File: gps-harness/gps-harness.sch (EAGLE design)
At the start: 7 parts

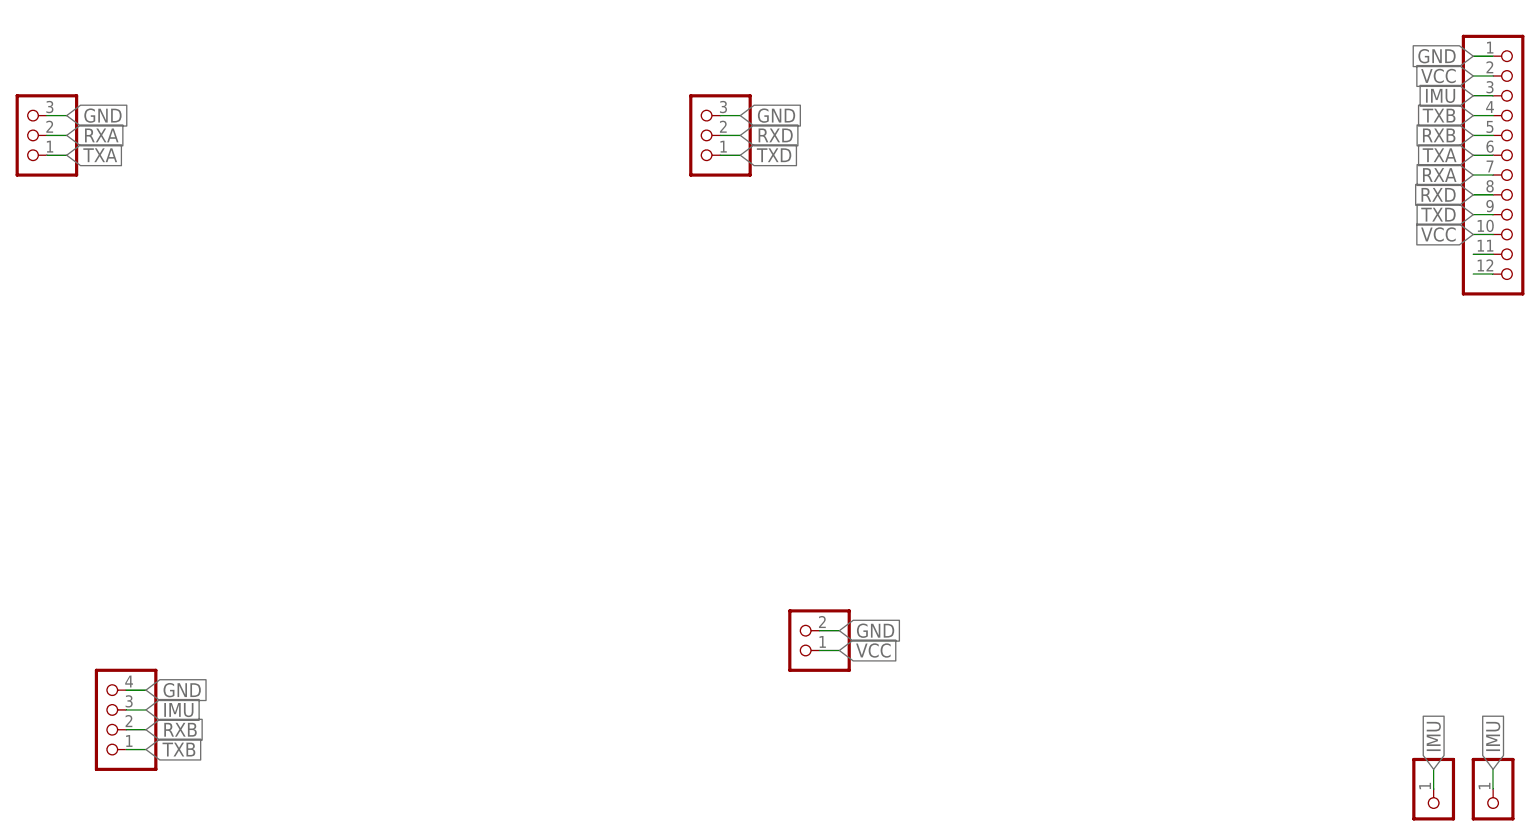
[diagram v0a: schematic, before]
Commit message: Add GND Plane
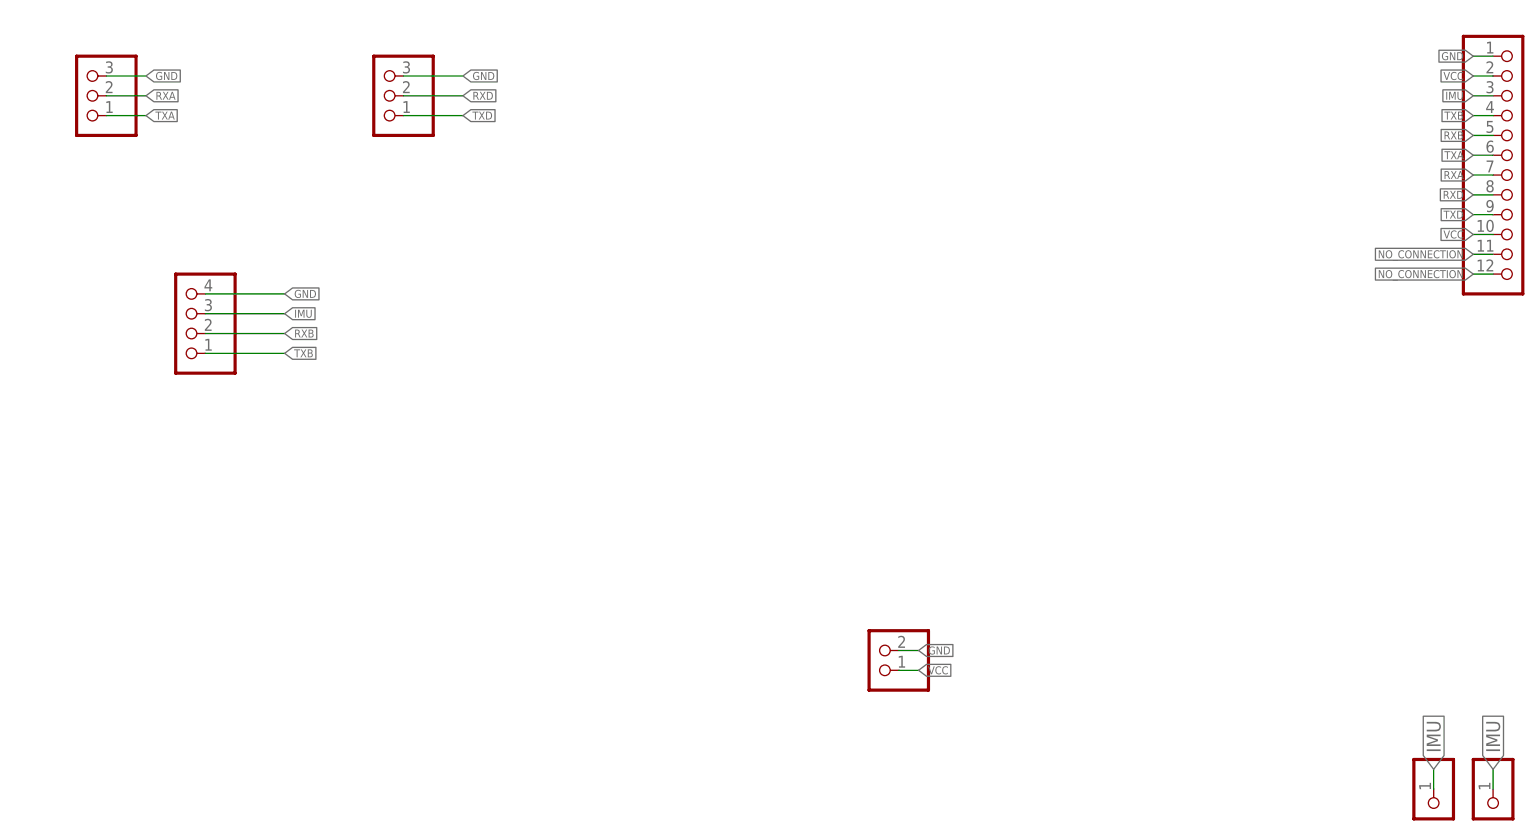
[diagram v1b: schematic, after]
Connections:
- removed net N$23: GPIO.11
- removed net N$24: GPIO.12
- new net NO_CONNECTION: GPIO.11, GPIO.12

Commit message: Add GND PLane & clearify the fastner of the right bottom driller, regorup rhe schematic
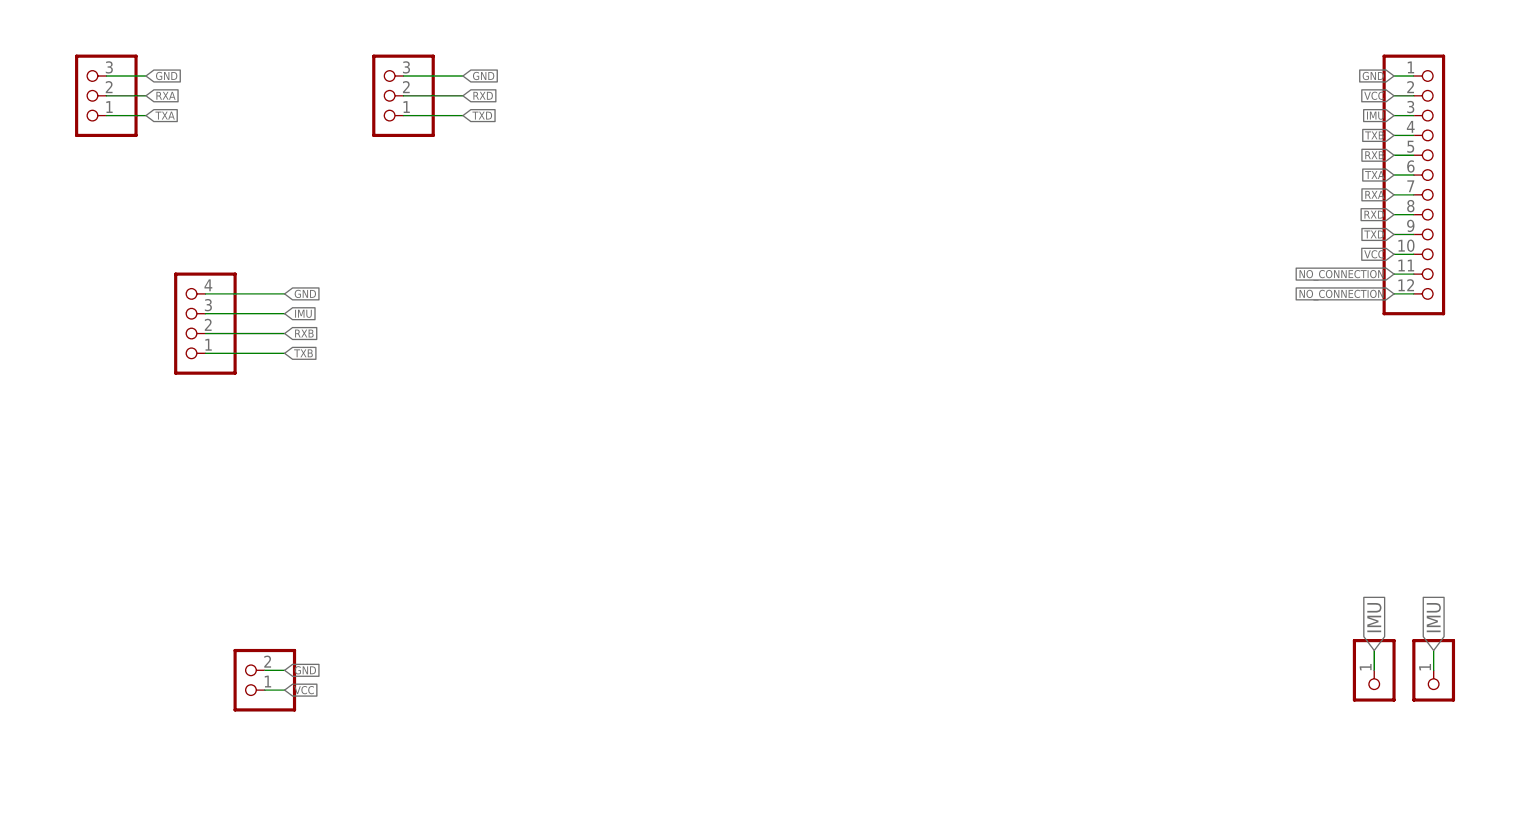
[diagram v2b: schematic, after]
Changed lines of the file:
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@@
 <attribute name="VALUE" x="59.69" y="157.48" size="1.778" layer="96" rot="R180"/>
 </instance>
-<instance part="BATTERY" gate="G$1" x="142.24" y="106.68" smashed="yes" rot="R180" grouprefs="BATTERY_POWER">
-<attribute name="VALUE" x="148.59" y="111.76" size="1.778" layer="96" rot="R180"/>
+<instance part="BATTERY" gate="G$1" x="60.96" y="104.14" smashed="yes" rot="R180" grouprefs="BATTERY_POWER">
+<attribute name="VALUE" x="67.31" y="109.22" size="1.778" layer="96" rot="R180"/>
 </instance>
-<instance part="GPIO" gate="G$1" x="223.52" y="170.18" smashed="yes" grouprefs="GPI/O">
-<attribute name="VALUE" x="217.17" y="149.86" size="1.778" layer="96"/>
+<instance part="GPIO" gate="G$1" x="213.36" y="167.64" smashed="yes" grouprefs="GPI/O">
+<attribute name="VALUE" x="207.01" y="147.32" size="1.778" layer="96"/>
 </instance>
-<instance part="IMU" gate="G$1" x="213.36" y="86.36" smashed="yes" rot="R270" grouprefs="IMU_TSY">
-<attribute name="VALUE" x="208.28" y="92.71" size="1.778" layer="96" rot="R270"/>
+<instance part="IMU" gate="G$1" x="205.74" y="101.6" smashed="yes" rot="R270" grouprefs="IMU_TSY">
+<attribute name="VALUE" x="200.66" y="107.95" size="1.778" layer="96" rot="R270"/>
 </instance>
-<instance part="TSY" gate="G$1" x="220.98" y="86.36" smashed="yes" rot="R270" grouprefs="IMU_TSY">
-<attribute name="VALUE" x="215.9" y="92.71" size="1.778" layer="96" rot="R270"/>
+<instance part="TSY" gate="G$1" x="213.36" y="101.6" smashed="yes" rot="R270" grouprefs="IMU_TSY">
+<attribute name="VALUE" x="208.28" y="107.95" size="1.778" layer="96" rot="R270"/>
 </instance>
 <instance part="FRAME1" gate="G$1" x="0" y="0" smashed="yes"/>
@@
 <segment>
 <pinref part="GPIO" gate="G$1" pin="1"/>
-<wire x1="220.98" y1="182.88" x2="218.44" y2="182.88" width="0.1524" layer="91" grouprefs="GPI/O"/>
-<label x="218.44" y="182.88" size="1.016" layer="95" rot="R180" xref="yes" grouprefs="GPI/O"/>
+<wire x1="210.82" y1="180.34" x2="208.28" y2="180.34" width="0.1524" layer="91" grouprefs="GPI/O"/>
+<label x="208.28" y="180.34" size="1.016" layer="95" rot="R180" xref="yes" grouprefs="GPI/O"/>
 </segment>
 <segment>
 <pinref part="BATTERY" gate="G$1" pin="2"/>
-<wire x1="144.78" y1="106.68" x2="147.32" y2="106.68" width="0.1524" layer="91" grouprefs="BATTERY_POWER"/>
-<label x="147.32" y="106.68" size="1.016" layer="95" xref="yes" grouprefs="BATTERY_POWER"/>
+<wire x1="63.5" y1="104.14" x2="66.04" y2="104.14" width="0.1524" layer="91" grouprefs="BATTERY_POWER"/>
+<label x="66.04" y="104.14" size="1.016" layer="95" xref="yes" grouprefs="BATTERY_POWER"/>
 </segment>
 </net>
@@
 <segment>
 <pinref part="GPIO" gate="G$1" pin="7"/>
-<wire x1="220.98" y1="167.64" x2="218.44" y2="167.64" width="0.1524" layer="91" grouprefs="GPI/O"/>
-<label x="218.44" y="167.64" size="1.016" layer="95" rot="R180" xref="yes" grouprefs="GPI/O"/>
+<wire x1="210.82" y1="165.1" x2="208.28" y2="165.1" width="0.1524" layer="91" grouprefs="GPI/O"/>
+<label x="208.28" y="165.1" size="1.016" layer="95" rot="R180" xref="yes" grouprefs="GPI/O"/>
 </segment>
 </net>
@@
 <segment>
 <pinref part="GPIO" gate="G$1" pin="6"/>
-<wire x1="220.98" y1="170.18" x2="218.44" y2="170.18" width="0.1524" layer="91" grouprefs="GPI/O"/>
-<label x="218.44" y="170.18" size="1.016" layer="95" rot="R180" xref="yes" grouprefs="GPI/O"/>
+<wire x1="210.82" y1="167.64" x2="208.28" y2="167.64" width="0.1524" layer="91" grouprefs="GPI/O"/>
+<label x="208.28" y="167.64" size="1.016" layer="95" rot="R180" xref="yes" grouprefs="GPI/O"/>
 </segment>
 </net>
@@
 <segment>
 <pinref part="GPIO" gate="G$1" pin="5"/>
-<wire x1="220.98" y1="172.72" x2="218.44" y2="172.72" width="0.1524" layer="91" grouprefs="GPI/O"/>
-<label x="218.44" y="172.72" size="1.016" layer="95" rot="R180" xref="yes" grouprefs="GPI/O"/>
+<wire x1="210.82" y1="170.18" x2="208.28" y2="170.18" width="0.1524" layer="91" grouprefs="GPI/O"/>
+<label x="208.28" y="170.18" size="1.016" layer="95" rot="R180" xref="yes" grouprefs="GPI/O"/>
 </segment>
 </net>
@@
 <segment>
 <pinref part="GPIO" gate="G$1" pin="4"/>
-<wire x1="220.98" y1="175.26" x2="218.44" y2="175.26" width="0.1524" layer="91" grouprefs="GPI/O"/>
-<label x="218.44" y="175.26" size="1.016" layer="95" rot="R180" xref="yes" grouprefs="GPI/O"/>
+<wire x1="210.82" y1="172.72" x2="208.28" y2="172.72" width="0.1524" layer="91" grouprefs="GPI/O"/>
+<label x="208.28" y="172.72" size="1.016" layer="95" rot="R180" xref="yes" grouprefs="GPI/O"/>
 </segment>
 </net>
@@
 <segment>
 <pinref part="BATTERY" gate="G$1" pin="1"/>
-<wire x1="144.78" y1="104.14" x2="147.32" y2="104.14" width="0.1524" layer="91" grouprefs="BATTERY_POWER"/>
-<label x="147.32" y="104.14" size="1.016" layer="95" xref="yes" grouprefs="BATTERY_POWER"/>
+<wire x1="63.5" y1="101.6" x2="66.04" y2="101.6" width="0.1524" layer="91" grouprefs="BATTERY_POWER"/>
+<label x="66.04" y="101.6" size="1.016" layer="95" xref="yes" grouprefs="BATTERY_POWER"/>
 </segment>
 <segment>
 <pinref part="GPIO" gate="G$1" pin="2"/>
-<wire x1="220.98" y1="180.34" x2="218.44" y2="180.34" width="0.1524" layer="91" grouprefs="GPI/O"/>
-<label x="218.44" y="180.34" size="1.016" layer="95" rot="R180" xref="yes" grouprefs="GPI/O"/>
+<wire x1="210.82" y1="177.8" x2="208.28" y2="177.8" width="0.1524" layer="91" grouprefs="GPI/O"/>
+<label x="208.28" y="177.8" size="1.016" layer="95" rot="R180" xref="yes" grouprefs="GPI/O"/>
 </segment>
 <segment>
 <pinref part="GPIO" gate="G$1" pin="10"/>
-<wire x1="220.98" y1="160.02" x2="218.44" y2="160.02" width="0.1524" layer="91" grouprefs="GPI/O"/>
-<label x="218.44" y="160.02" size="1.016" layer="95" rot="R180" xref="yes" grouprefs="GPI/O"/>
+<wire x1="210.82" y1="157.48" x2="208.28" y2="157.48" width="0.1524" layer="91" grouprefs="GPI/O"/>
+<label x="208.28" y="157.48" size="1.016" layer="95" rot="R180" xref="yes" grouprefs="GPI/O"/>
 </segment>
 </net>
@@
 <segment>
 <pinref part="GPIO" gate="G$1" pin="9"/>
-<wire x1="220.98" y1="162.56" x2="218.44" y2="162.56" width="0.1524" layer="91" grouprefs="GPI/O"/>
-<label x="218.44" y="162.56" size="1.016" layer="95" rot="R180" xref="yes" grouprefs="GPI/O"/>
+<wire x1="210.82" y1="160.02" x2="208.28" y2="160.02" width="0.1524" layer="91" grouprefs="GPI/O"/>
+<label x="208.28" y="160.02" size="1.016" layer="95" rot="R180" xref="yes" grouprefs="GPI/O"/>
 </segment>
 </net>
@@
 <segment>
 <pinref part="GPIO" gate="G$1" pin="8"/>
-<wire x1="220.98" y1="165.1" x2="218.44" y2="165.1" width="0.1524" layer="91" grouprefs="GPI/O"/>
-<label x="218.44" y="165.1" size="1.016" layer="95" rot="R180" xref="yes" grouprefs="GPI/O"/>
+<wire x1="210.82" y1="162.56" x2="208.28" y2="162.56" width="0.1524" layer="91" grouprefs="GPI/O"/>
+<label x="208.28" y="162.56" size="1.016" layer="95" rot="R180" xref="yes" grouprefs="GPI/O"/>
 </segment>
 </net>
@@
 <segment>
 <pinref part="GPIO" gate="G$1" pin="3"/>
-<wire x1="220.98" y1="177.8" x2="218.44" y2="177.8" width="0.1524" layer="91" grouprefs="GPI/O"/>
-<label x="218.44" y="177.8" size="1.016" layer="95" rot="R180" xref="yes" grouprefs="GPI/O"/>
+<wire x1="210.82" y1="175.26" x2="208.28" y2="175.26" width="0.1524" layer="91" grouprefs="GPI/O"/>
+<label x="208.28" y="175.26" size="1.016" layer="95" rot="R180" xref="yes" grouprefs="GPI/O"/>
 </segment>
 <segment>
@@
 <segment>
 <pinref part="IMU" gate="G$1" pin="1"/>
-<wire x1="213.36" y1="88.9" x2="213.36" y2="91.44" width="0.1524" layer="91" grouprefs="IMU_TSY"/>
-<label x="213.36" y="91.44" size="1.778" layer="95" rot="R90" xref="yes" grouprefs="IMU_TSY"/>
+<wire x1="205.74" y1="104.14" x2="205.74" y2="106.68" width="0.1524" layer="91" grouprefs="IMU_TSY"/>
+<label x="205.74" y="106.68" size="1.778" layer="95" rot="R90" xref="yes" grouprefs="IMU_TSY"/>
 </segment>
 <segment>
 <pinref part="TSY" gate="G$1" pin="1"/>
-<wire x1="220.98" y1="88.9" x2="220.98" y2="91.44" width="0.1524" layer="91" grouprefs="IMU_TSY"/>
-<label x="220.98" y="91.44" size="1.778" layer="95" rot="R90" xref="yes" grouprefs="IMU_TSY"/>
+<wire x1="213.36" y1="104.14" x2="213.36" y2="106.68" width="0.1524" layer="91" grouprefs="IMU_TSY"/>
+<label x="213.36" y="106.68" size="1.778" layer="95" rot="R90" xref="yes" grouprefs="IMU_TSY"/>
 </segment>
 </net>
@@
 <segment>
 <pinref part="GPIO" gate="G$1" pin="11"/>
-<wire x1="220.98" y1="157.48" x2="218.44" y2="157.48" width="0.1524" layer="91" grouprefs="GPI/O"/>
-<label x="218.44" y="157.48" size="1.016" layer="95" rot="R180" xref="yes"/>
+<wire x1="210.82" y1="154.94" x2="208.28" y2="154.94" width="0.1524" layer="91" grouprefs="GPI/O"/>
+<label x="208.28" y="154.94" size="1.016" layer="95" rot="R180" xref="yes"/>
 </segment>
 <segment>
 <pinref part="GPIO" gate="G$1" pin="12"/>
-<wire x1="220.98" y1="154.94" x2="218.44" y2="154.94" width="0.1524" layer="91" grouprefs="GPI/O"/>
-<label x="218.44" y="154.94" size="1.016" layer="95" rot="R180" xref="yes"/>
+<wire x1="210.82" y1="152.4" x2="208.28" y2="152.4" width="0.1524" layer="91" grouprefs="GPI/O"/>
+<label x="208.28" y="152.4" size="1.016" layer="95" rot="R180" xref="yes"/>
 </segment>
 </net>

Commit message: Modify the place of the left bottom mounting hole; Unify the width of the wires; clear up the GND line since there's a ground plane
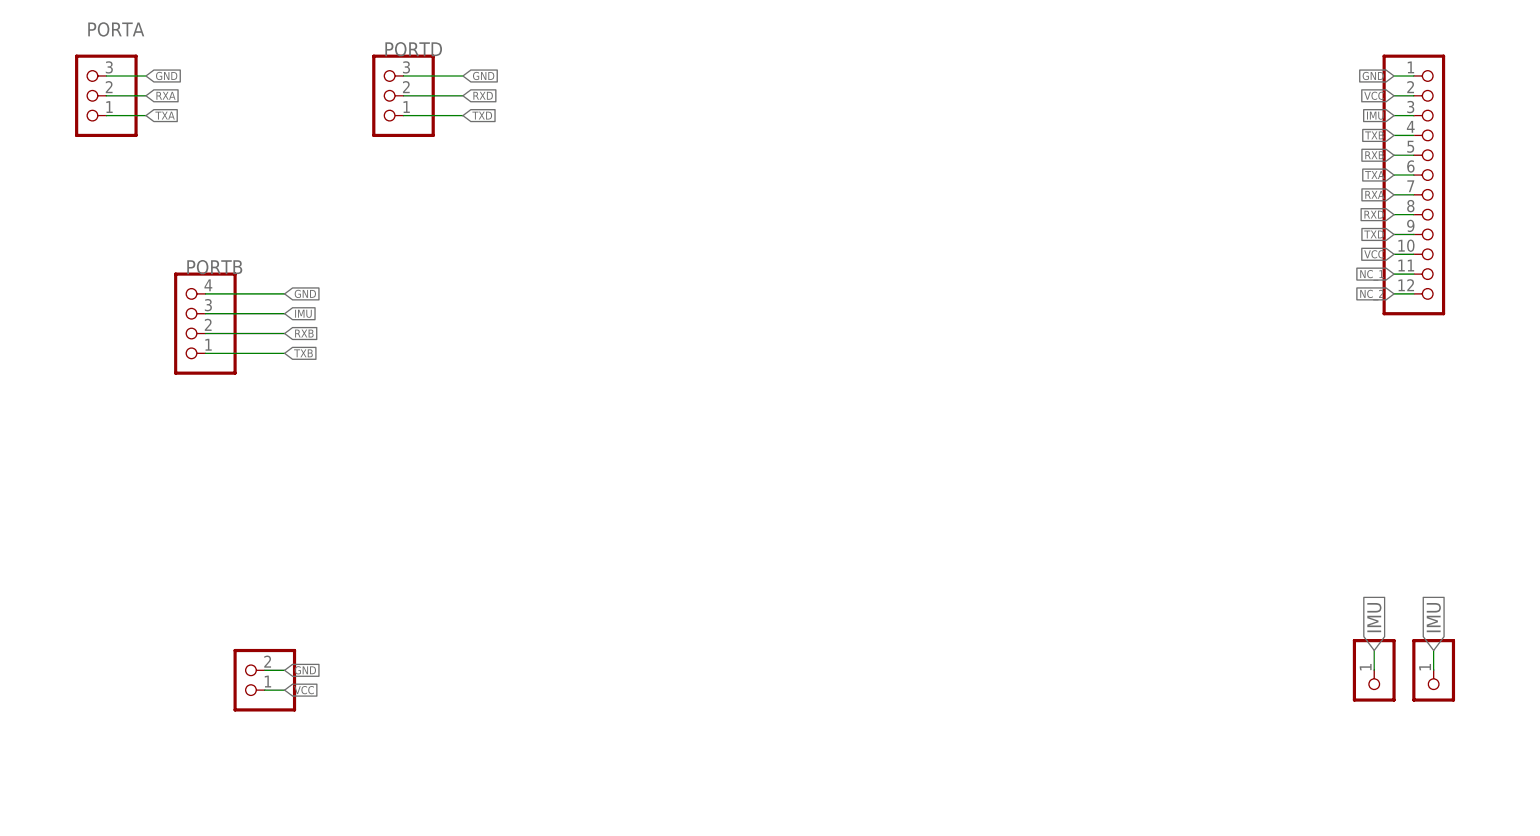
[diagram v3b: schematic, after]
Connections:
- removed net NO_CONNECTION: GPIO.11, GPIO.12
- new net NC_1: GPIO.11
- new net NC_2: GPIO.12
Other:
- note added: "PORTA"
- note added: "PORTB"
- note added: "PORTD"
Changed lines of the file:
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@@
 <sheet>
 <plain>
+<text x="40.64" y="185.42" size="1.778" layer="95">PORTA</text>
+<text x="53.34" y="154.94" size="1.778" layer="95">PORTB</text>
+<text x="78.74" y="182.88" size="1.778" layer="95">PORTD</text>
 </plain>
 <instances>
@@
 </segment>
 </net>
-<net name="NO_CONNECTION" class="0">
+<net name="NC_1" class="0">
 <segment>
 <pinref part="GPIO" gate="G$1" pin="11"/>
@@
 <label x="208.28" y="154.94" size="1.016" layer="95" rot="R180" xref="yes"/>
 </segment>
+</net>
+<net name="NC_2" class="0">
 <segment>
 <pinref part="GPIO" gate="G$1" pin="12"/>
